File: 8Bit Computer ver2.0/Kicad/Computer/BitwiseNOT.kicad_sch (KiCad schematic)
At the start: 5 parts, among them IC10 SN74HCS14DR, IC13 SN74HCS14DR, IC41 SN74LVC1G14DBVR, IC44 SN74HCS74DR, IC45 SN74HCS574DGSR

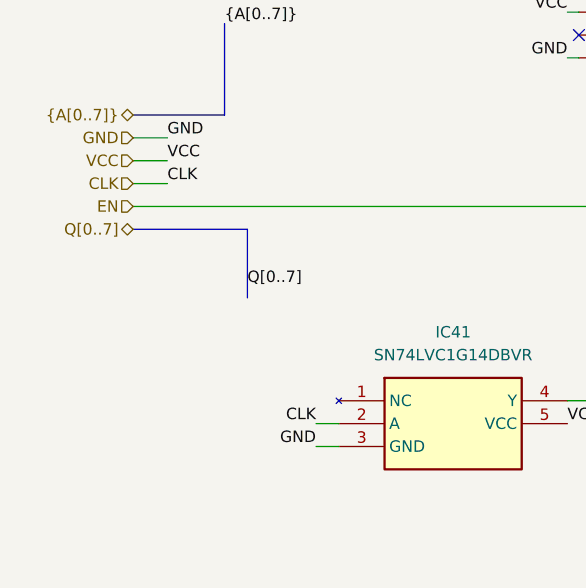
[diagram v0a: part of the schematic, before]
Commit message: Kicad,parts
Kicad:
added FlagRegister
began Inc, Comp
parts:
added comparator for P>Q 682
added faster sram 12ns AS7C
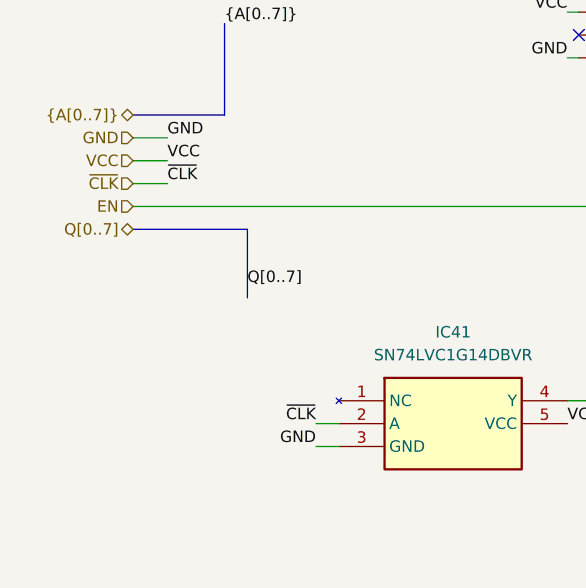
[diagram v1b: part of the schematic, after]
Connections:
- net CLK renamed ~{CLK}
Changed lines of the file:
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@@
 		)
 	)
-	(label "CLK"
+	(label "~{CLK}"
 		(at 64.77 134.62 180)
 		(effects
@@
 		)
 	)
-	(label "CLK"
+	(label "~{CLK}"
 		(at 48.26 107.95 0)
 		(effects
@@
 		)
 	)
-	(hierarchical_label "CLK"
+	(hierarchical_label "~{CLK}"
 		(shape input)
 		(at 44.45 107.95 180)

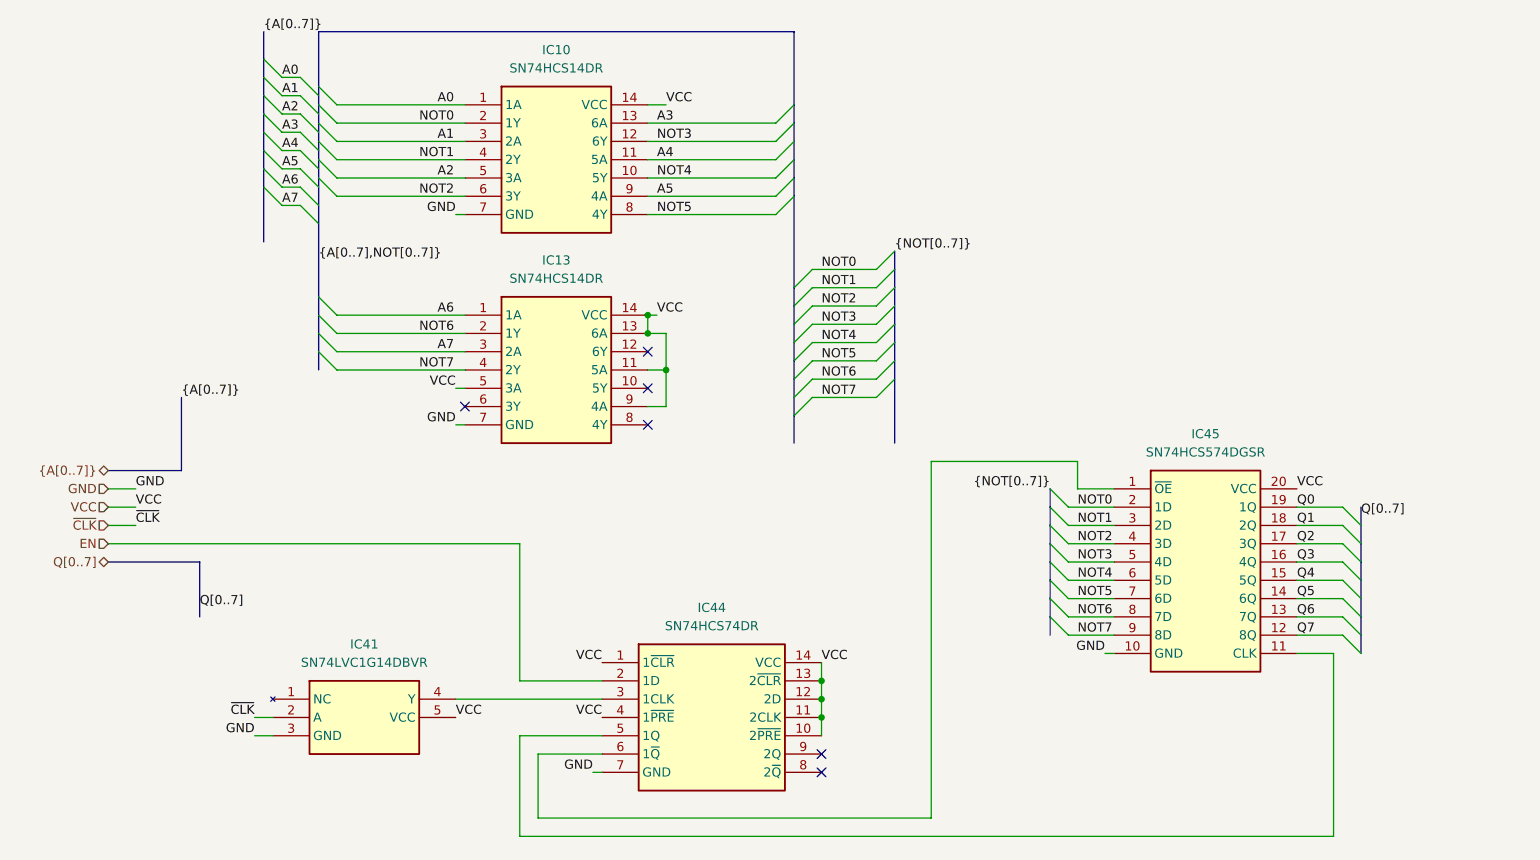
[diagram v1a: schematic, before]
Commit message: parts,Kicad
parts:
changed 8xDlatch HCS to ABT 574
waiting for SRAM CAD Model
Kicad:
imported AHC types of ICs
added ProgrammeCounter
finished Comparator
changed all HCS to AHC except 3in OR ->no AHC Version
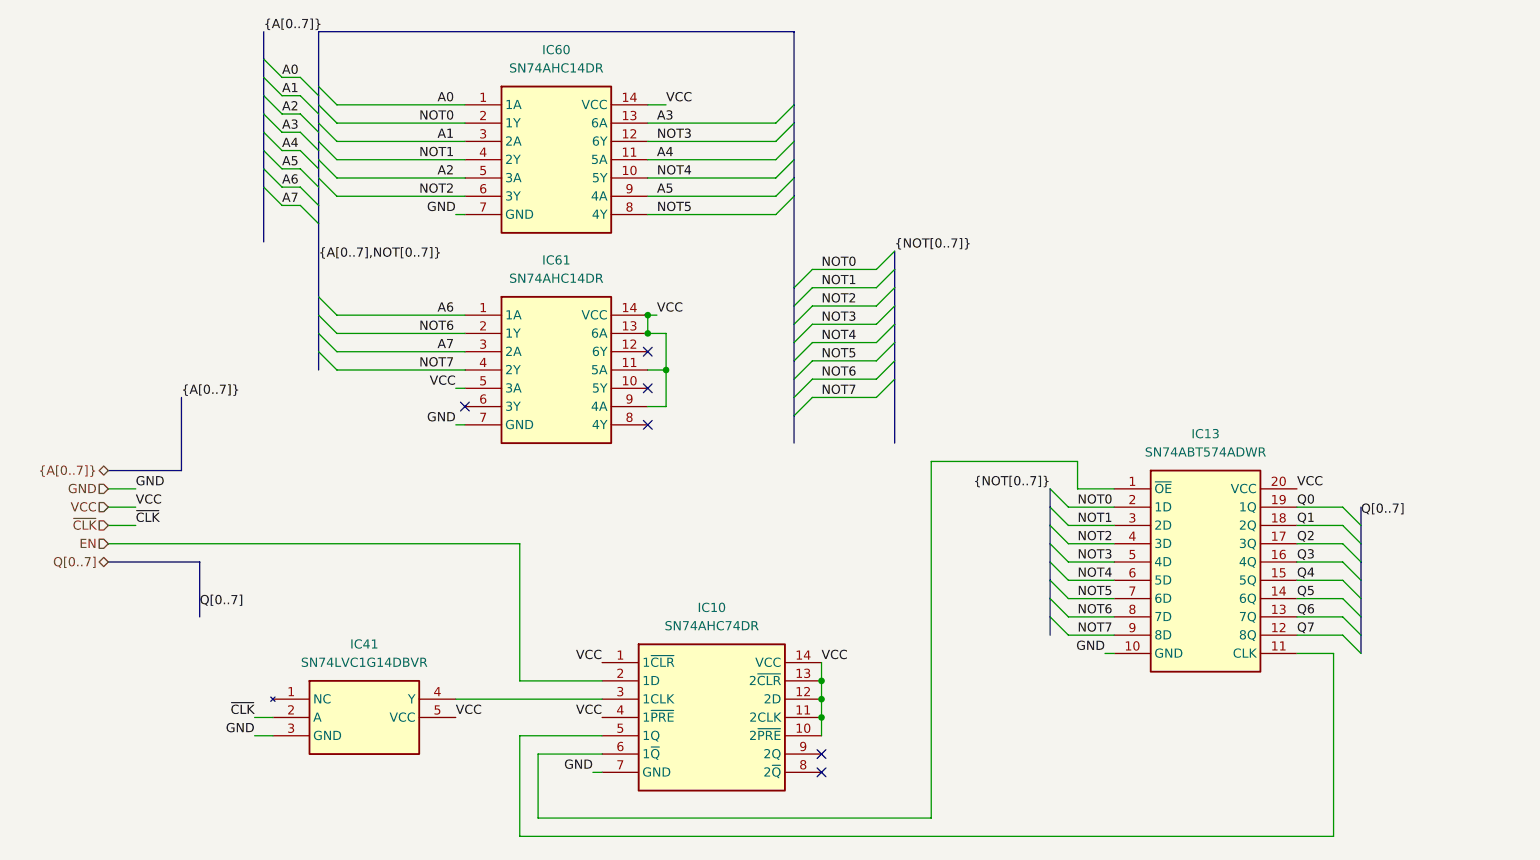
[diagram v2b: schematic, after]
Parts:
- removed IC10, IC13: SN74HCS14DR, Samacsys:SOIC127P600X175-14N, symbol Samacsys:SN74HCS14DR
- removed IC44: SN74HCS74DR, Samacsys:SOIC127P600X175-14N, symbol Samacsys:SN74HCS74DR
- removed IC45: SN74HCS574DGSR, Samacsys:SOP50P490X110-20N, symbol Samacsys:SN74HCS574DGSR
- added IC10: SN74AHC74DR, Samacsys:SOIC127P600X175-14N, symbol Samacsys:SN74AHC74DR
- added IC13: SN74ABT574ADWR, Samacsys:SOIC127P1030X265-20N, symbol Samacsys:SN74ABT574ADWR
- added IC60, IC61: SN74AHC14DR, Samacsys:SOIC127P600X175-14N, symbol Samacsys:SN74AHC14DR
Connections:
- net A0: now also IC60.1 (1A)
- net A1: now also IC60.3 (2A)
- net A2: now also IC60.5 (3A)
- net A3: now also IC60.13 (6A)
- net A4: now also IC60.11 (5A)
- net A5: now also IC60.9 (4A)
- net A6: now also IC61.1 (1A)
- net A7: now also IC61.3 (2A)
- net EN: now also IC10.2 (1D)
- net GND: now also IC10.7 (GND), IC13.10 (GND), IC60.7 (GND), IC61.7 (GND)
- net NOT0: now also IC13.2 (1D), IC60.2 (1Y)
- net NOT1: now also IC13.3 (2D), IC60.4 (2Y)
- net NOT2: now also IC13.4 (3D), IC60.6 (3Y)
- net NOT3: now also IC13.5 (4D), IC60.12 (6Y)
- net NOT4: now also IC13.6 (5D), IC60.10 (5Y)
- net NOT5: now also IC13.7 (6D), IC60.8 (4Y)
- net NOT6: now also IC13.8 (7D), IC61.2 (1Y)
- net NOT7: now also IC13.9 (8D), IC61.4 (2Y)
- net Q0: now also IC13.19 (1Q)
- net Q1: now also IC13.18 (2Q)
- net Q2: now also IC13.17 (3Q)
- net Q3: now also IC13.16 (4Q)
- net Q4: now also IC13.15 (5Q)
- net Q5: now also IC13.14 (6Q)
- net Q6: now also IC13.13 (7Q)
- net Q7: now also IC13.12 (8Q)
- net VCC: now also IC10.1 (1~{CLR}), IC10.10 (2~{PRE}), IC10.11 (2CLK), IC10.12 (2D), IC10.13 (2~{CLR}), IC10.14 (VCC), IC10.4 (1~{PRE}), IC13.20 (VCC), IC60.14 (VCC), IC61.11 (5A), IC61.13 (6A), IC61.14 (VCC), IC61.5 (3A), IC61.9 (4A)
- net at IC41.4 (Y): now also IC10.3 (1CLK)
- new net: IC10.5 (1Q), IC13.11 (CLK)
- new net: IC10.6 (1~{Q}), IC13.1 (~{OE})

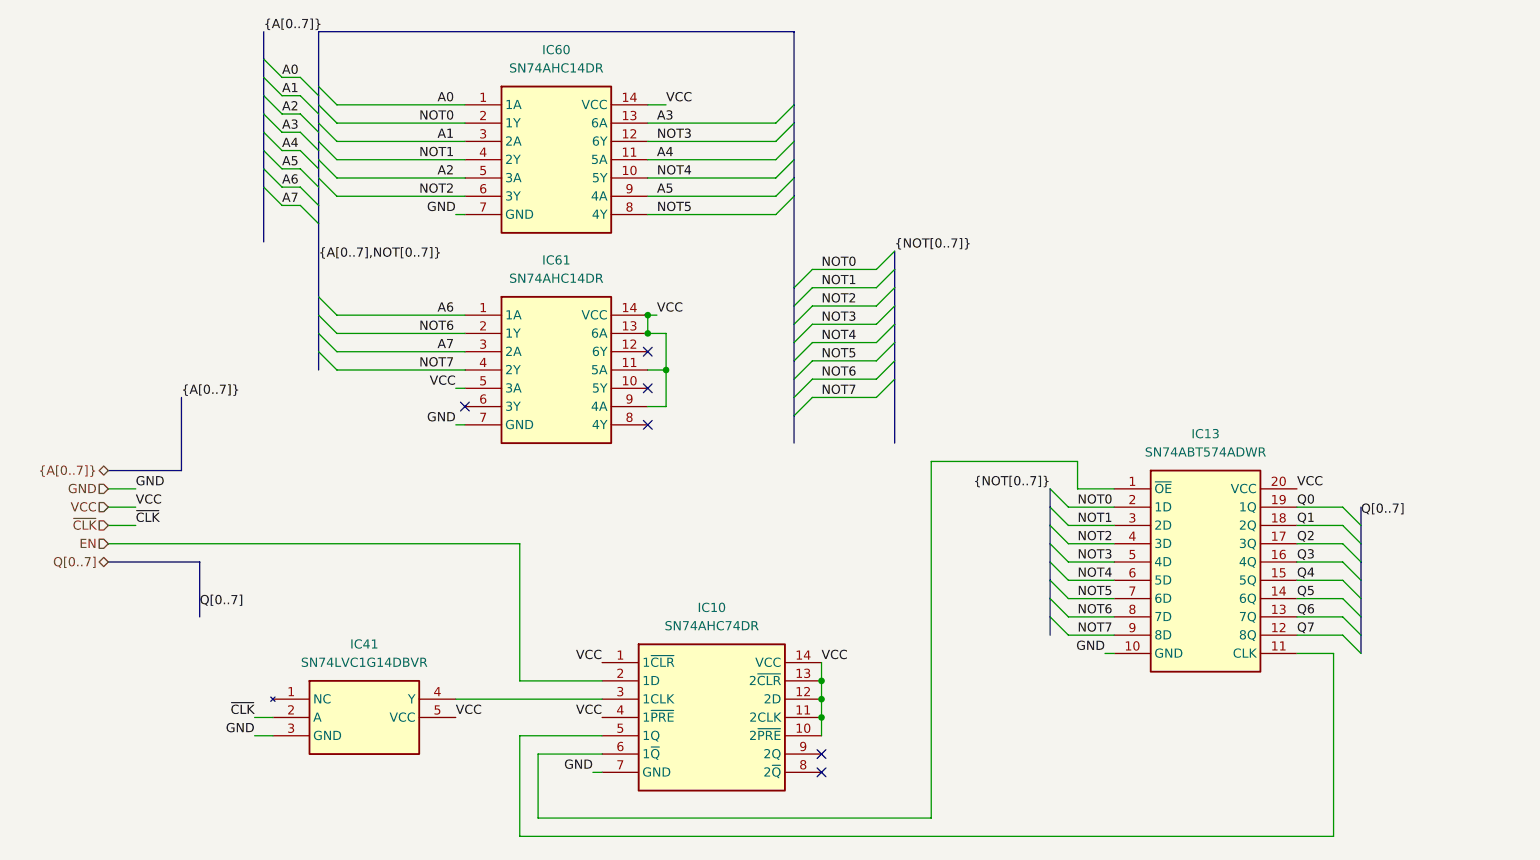
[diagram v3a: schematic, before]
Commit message: Kicad, parts
Parts:
added Leds
Kicad:
added Input Output
changed Q bus to DAT bus
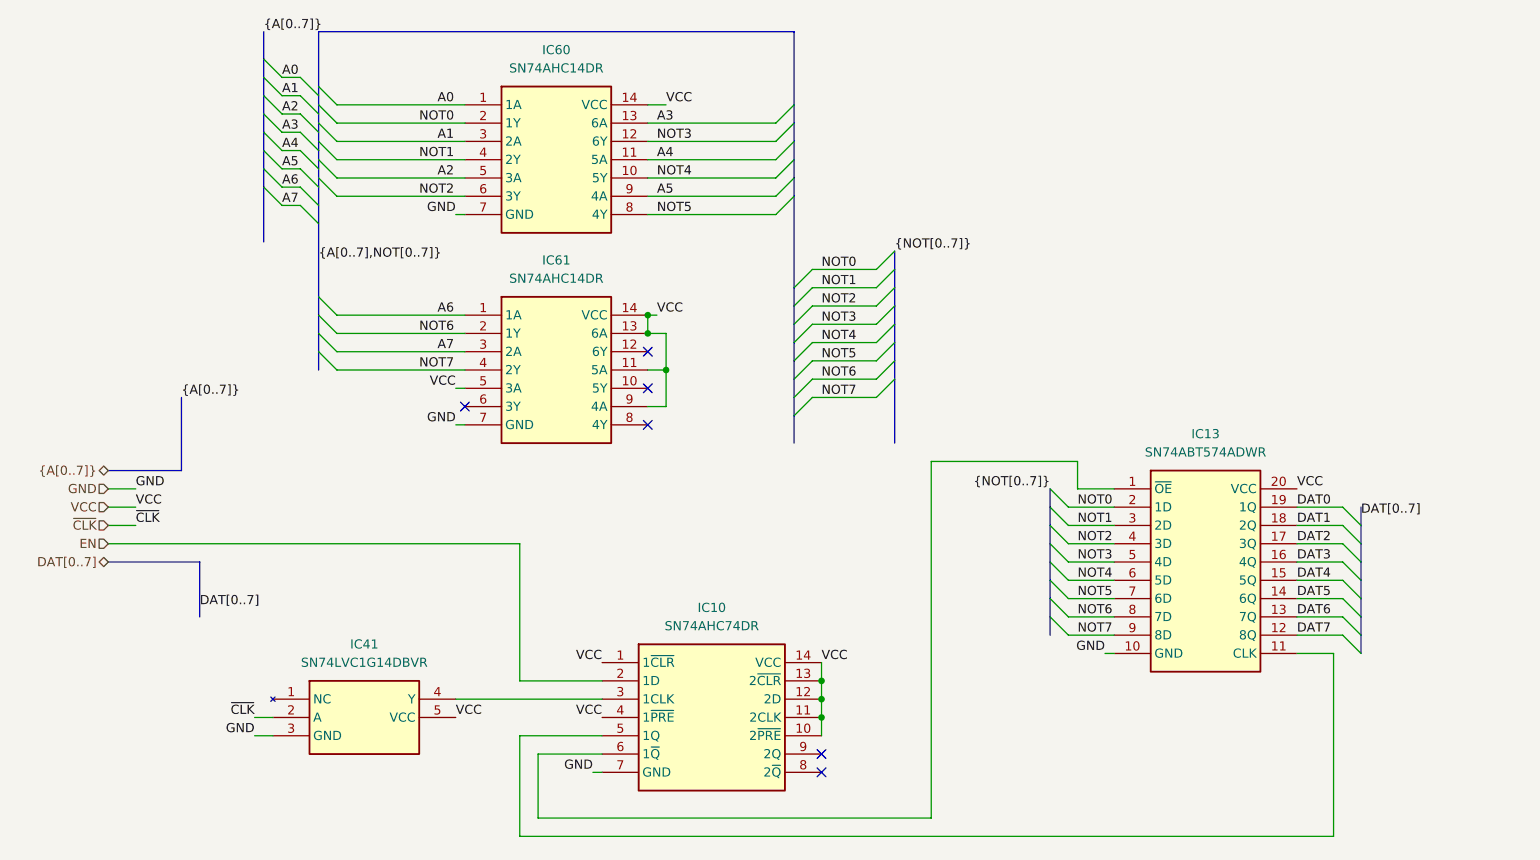
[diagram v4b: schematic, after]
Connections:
- net Q0 renamed DAT0
- net Q1 renamed DAT1
- net Q2 renamed DAT2
- net Q3 renamed DAT3
- net Q4 renamed DAT4
- net Q5 renamed DAT5
- net Q6 renamed DAT6
- net Q7 renamed DAT7
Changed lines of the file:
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@@
 		)
 	)
-	(label "Q6"
+	(label "DAT6"
 		(at 209.55 120.65 0)
 		(effects
@@
 		)
 	)
-	(label "Q5"
+	(label "DAT5"
 		(at 209.55 118.11 0)
 		(effects
@@
 		)
 	)
-	(label "Q2"
+	(label "DAT2"
 		(at 209.55 110.49 0)
 		(effects
@@
 		)
 	)
-	(label "Q[0..7]"
+	(label "DAT[0..7]"
 		(at 218.44 106.68 0)
 		(effects
@@
 		)
 	)
-	(label "Q0"
+	(label "DAT0"
 		(at 209.55 105.41 0)
 		(effects
@@
 		)
 	)
-	(label "Q7"
+	(label "DAT7"
 		(at 209.55 123.19 0)
 		(effects
@@
 		)
 	)
-	(label "Q3"
+	(label "DAT3"
 		(at 209.55 113.03 0)
 		(effects
@@
 		)
 	)
-	(label "Q4"
+	(label "DAT4"
 		(at 209.55 115.57 0)
 		(effects
@@
 		)
 	)
-	(label "Q1"
+	(label "DAT1"
 		(at 209.55 107.95 0)
 		(effects
@@
 		)
 	)
-	(label "Q[0..7]"
+	(label "DAT[0..7]"
 		(at 57.15 119.38 0)
 		(effects
@@
 		)
 	)
-	(hierarchical_label "Q[0..7]"
+	(hierarchical_label "DAT[0..7]"
 		(shape tri_state)
 		(at 44.45 113.03 180)

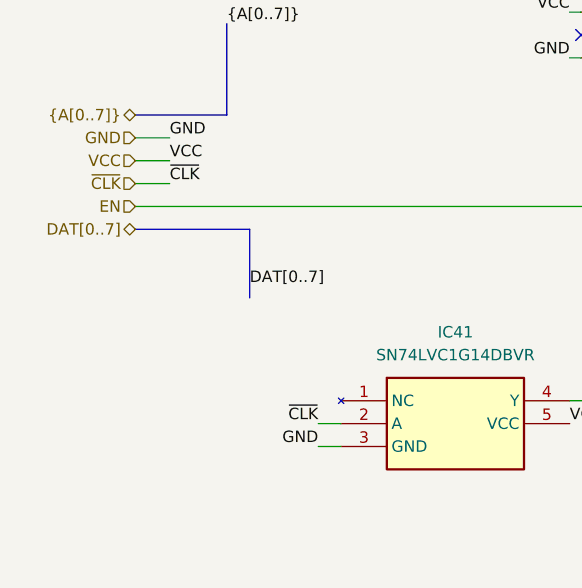
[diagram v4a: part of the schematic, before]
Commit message: Kicad, parts
parts:
added USB C PD Triggerboard
added Delay Chip for 90ns
added Push Button
Kicad:
added USB C PD Triggerboard
added rising edge detector via Delay and Xor for Accept Push Button
added VBUS net
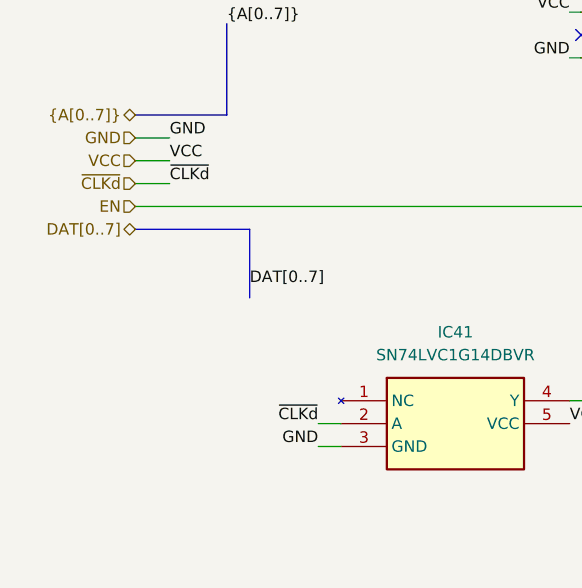
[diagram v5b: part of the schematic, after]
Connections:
- net ~{CLK} renamed ~{CLKd}
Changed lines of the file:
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@@
 		)
 	)
-	(label "~{CLK}"
+	(label "~{CLKd}"
 		(at 64.77 134.62 180)
 		(effects
@@
 		)
 	)
-	(label "~{CLK}"
+	(label "~{CLKd}"
 		(at 48.26 107.95 0)
 		(effects
@@
 		)
 	)
-	(hierarchical_label "~{CLK}"
+	(hierarchical_label "~{CLKd}"
 		(shape input)
 		(at 44.45 107.95 180)
